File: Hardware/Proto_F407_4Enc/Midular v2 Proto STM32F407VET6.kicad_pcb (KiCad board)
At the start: 4 copper layers, 94 x 94 mm, 109 parts, among them J1 Conn_01x03_Male, J10 Conn_01x04, J11 Conn_01x04, J12 Conn_01x04, J13 Conn_01x04, J14 Conn_01x08, J15 Conn_01x08, J16 Conn_01x06, J17 Conn_01x04, J18 Conn_01x01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

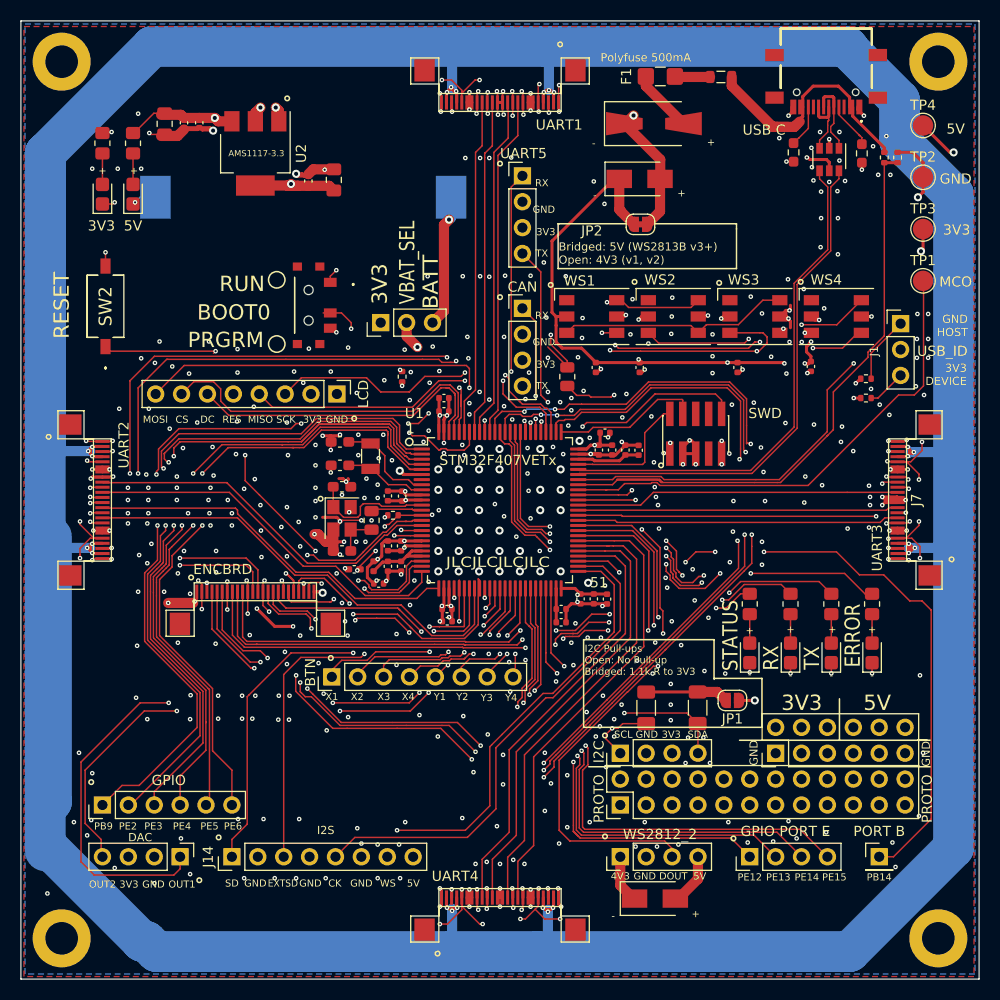
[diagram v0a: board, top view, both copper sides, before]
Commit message: minor label changes in schematic, added schematic + board image plots
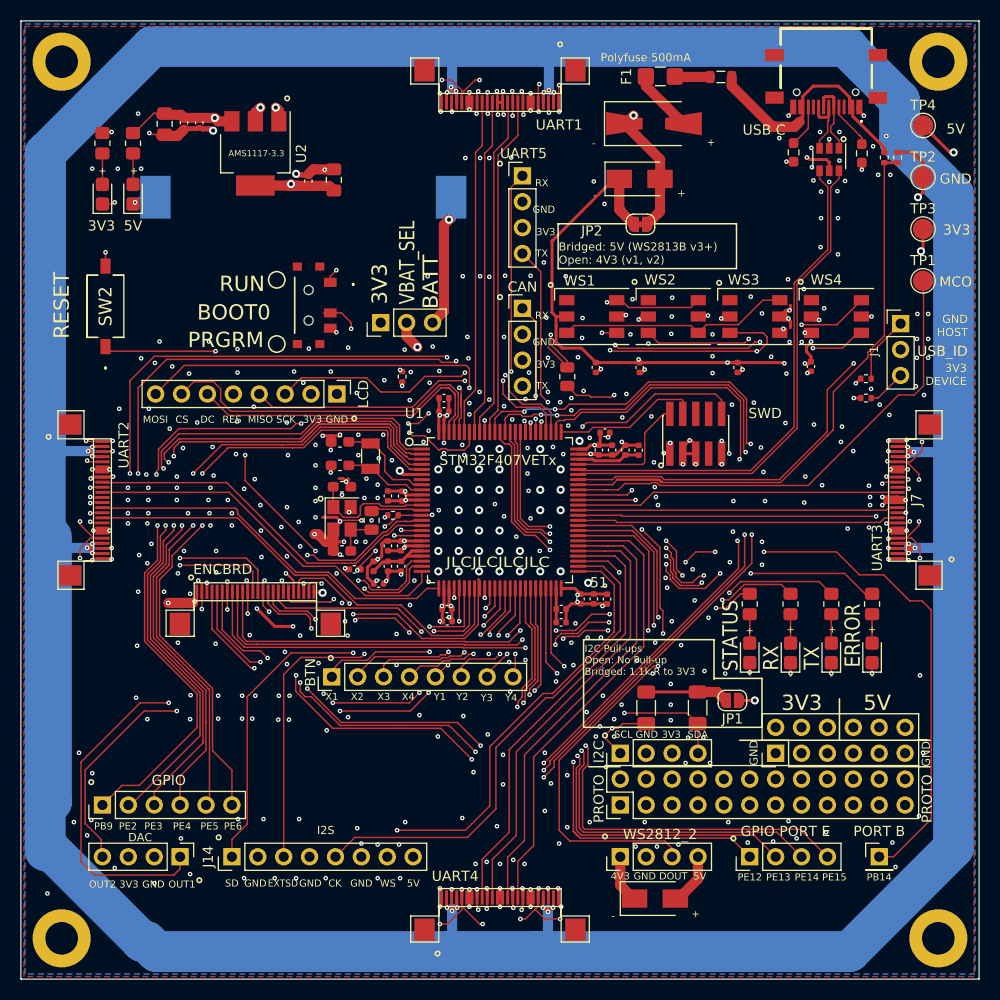
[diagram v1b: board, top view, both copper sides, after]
